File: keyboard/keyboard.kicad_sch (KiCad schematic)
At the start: 201 parts, among them U1 Raspberry_Pi_Pico

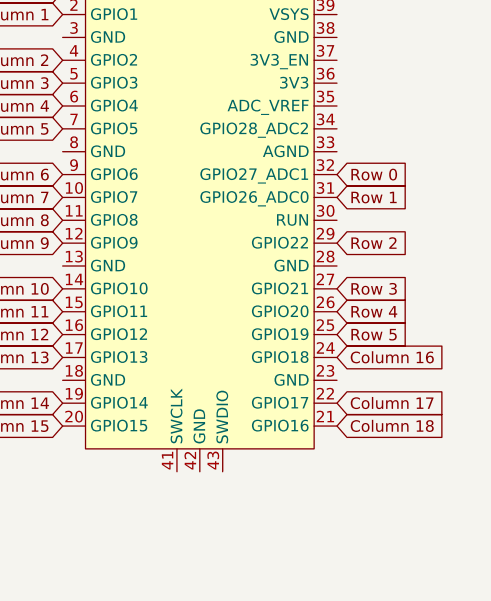
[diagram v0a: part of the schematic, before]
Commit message: Updated PCB design with a different MCU mount in order to reduce the total height
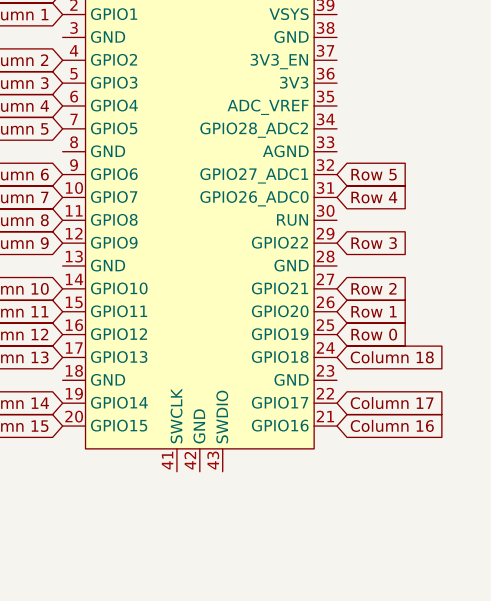
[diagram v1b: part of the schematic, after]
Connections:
- net Column 16: now also U1.21 (GPIO16); no longer U1.24 (GPIO18)
- net Column 18: now also U1.24 (GPIO18); no longer U1.21 (GPIO16)
- net Row 0: now also U1.25 (GPIO19); no longer U1.32 (GPIO27_ADC1)
- net Row 1: now also U1.26 (GPIO20); no longer U1.31 (GPIO26_ADC0)
- net Row 2: now also U1.27 (GPIO21); no longer U1.29 (GPIO22)
- net Row 3: now also U1.29 (GPIO22); no longer U1.27 (GPIO21)
- net Row 4: now also U1.31 (GPIO26_ADC0); no longer U1.26 (GPIO20)
- net Row 5: now also U1.32 (GPIO27_ADC1); no longer U1.25 (GPIO19)
